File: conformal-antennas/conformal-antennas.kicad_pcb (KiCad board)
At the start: 2 copper layers, 1 part, among them J1 Conn_Coaxial

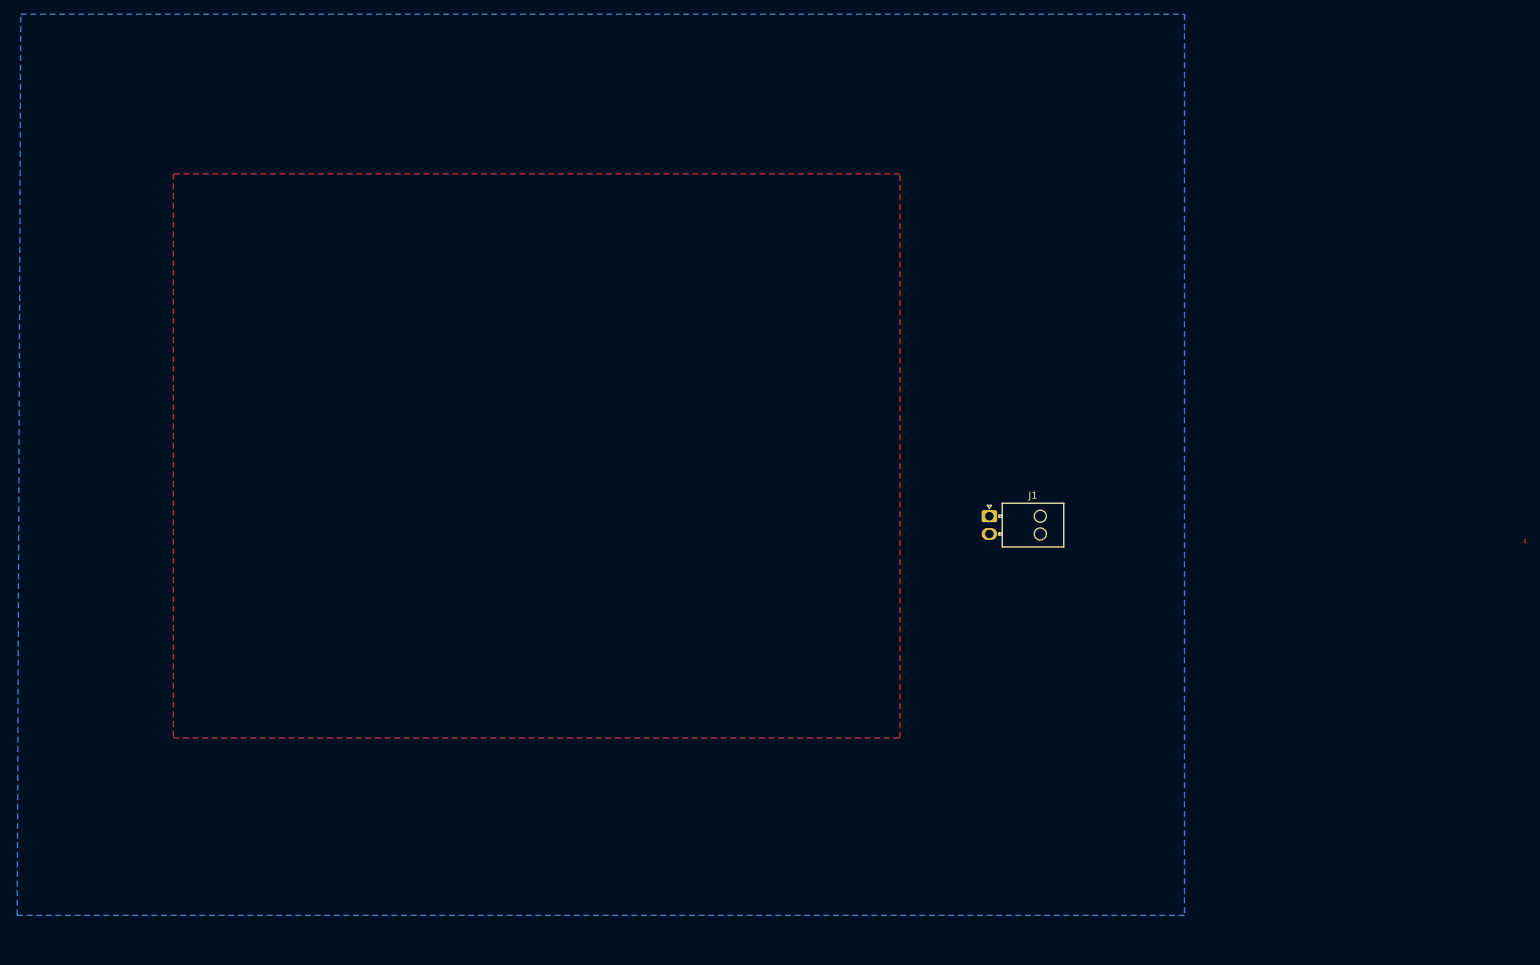
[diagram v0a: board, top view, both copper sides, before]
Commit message: changed coaxial connector to edge mount
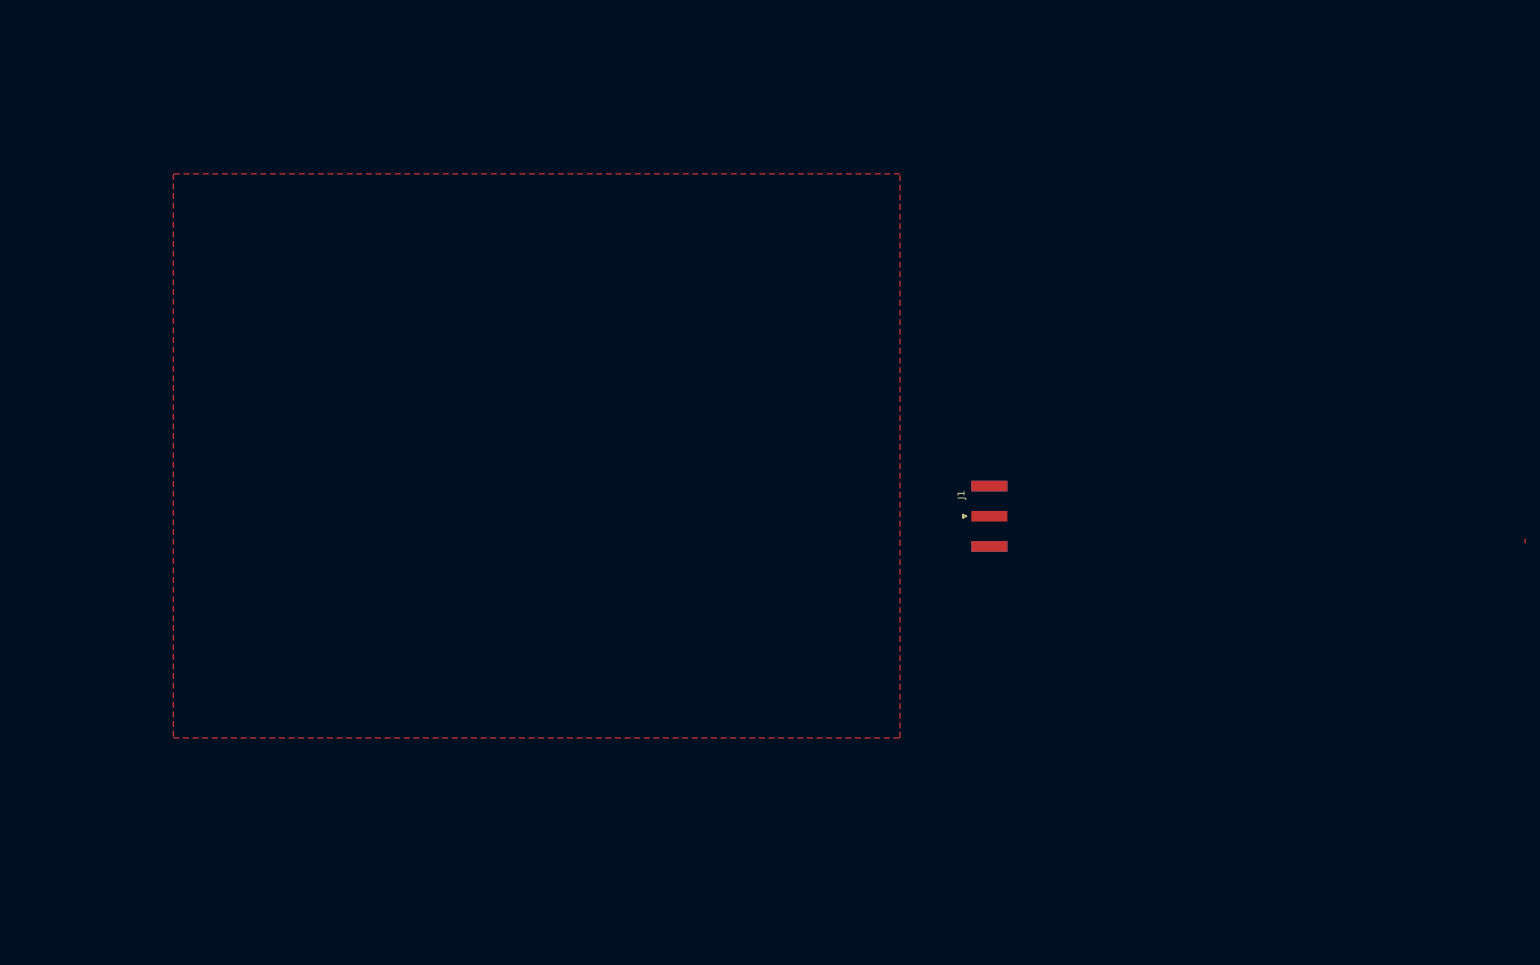
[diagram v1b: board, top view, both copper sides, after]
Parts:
- J1: footprint iclr:Molex_Nano-Fit_105313-xx02_1x02_P2.50mm_Horizontal -> Connector_Coaxial:SMA_Amphenol_132289_EdgeMount
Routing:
- removed copper zone on B.Cu, net GND

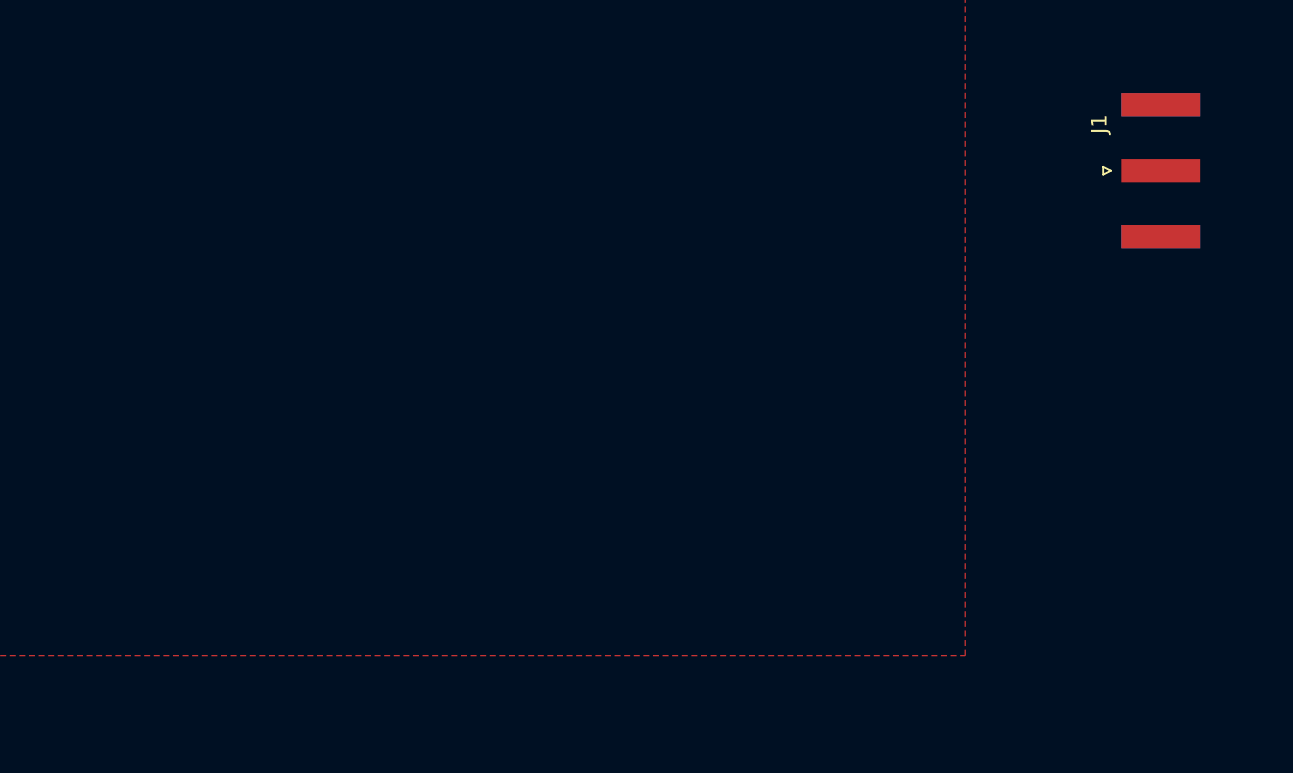
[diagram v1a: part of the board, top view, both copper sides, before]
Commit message: Simple path and tracks and SMA connector
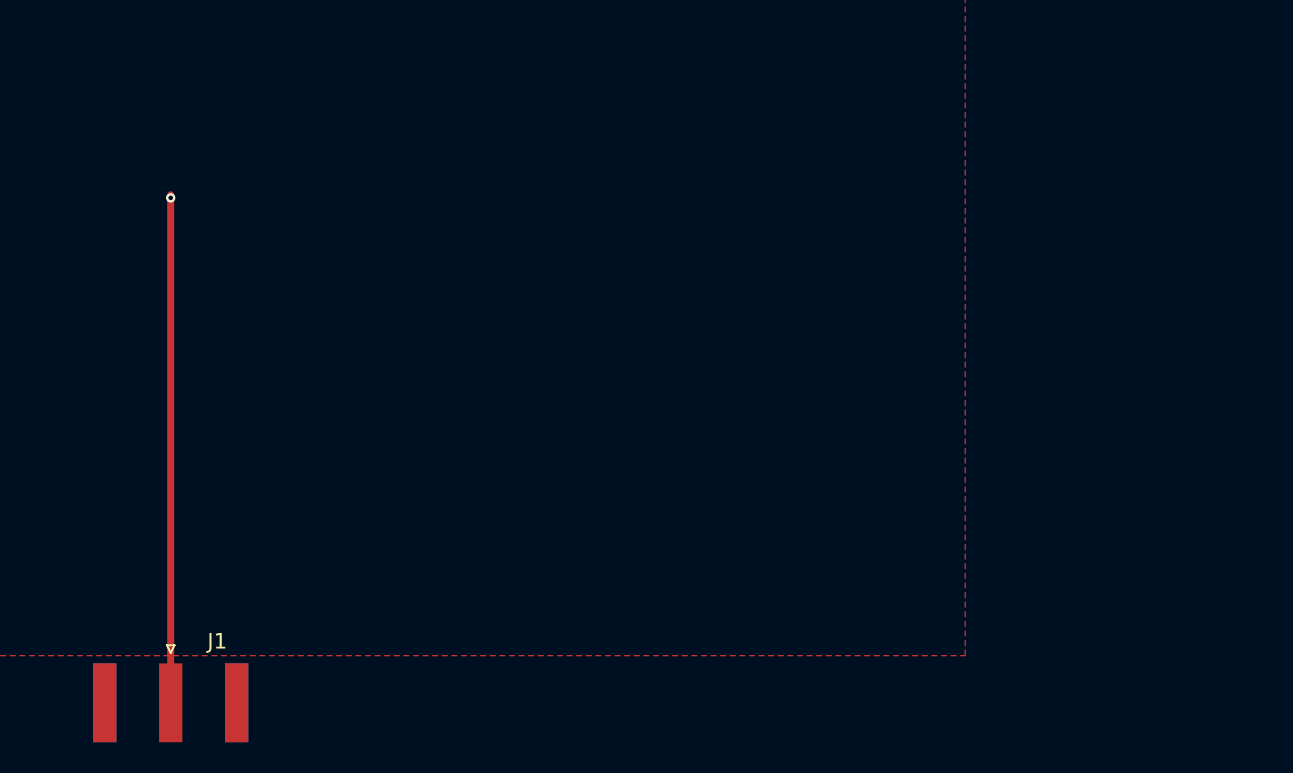
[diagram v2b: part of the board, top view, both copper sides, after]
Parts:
- moved J1 72.4 mm to (108.2, 149.5), turned to -90 degrees
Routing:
- net /Signal: track 0.00 -> 32.7 mm, vias 0 -> 1

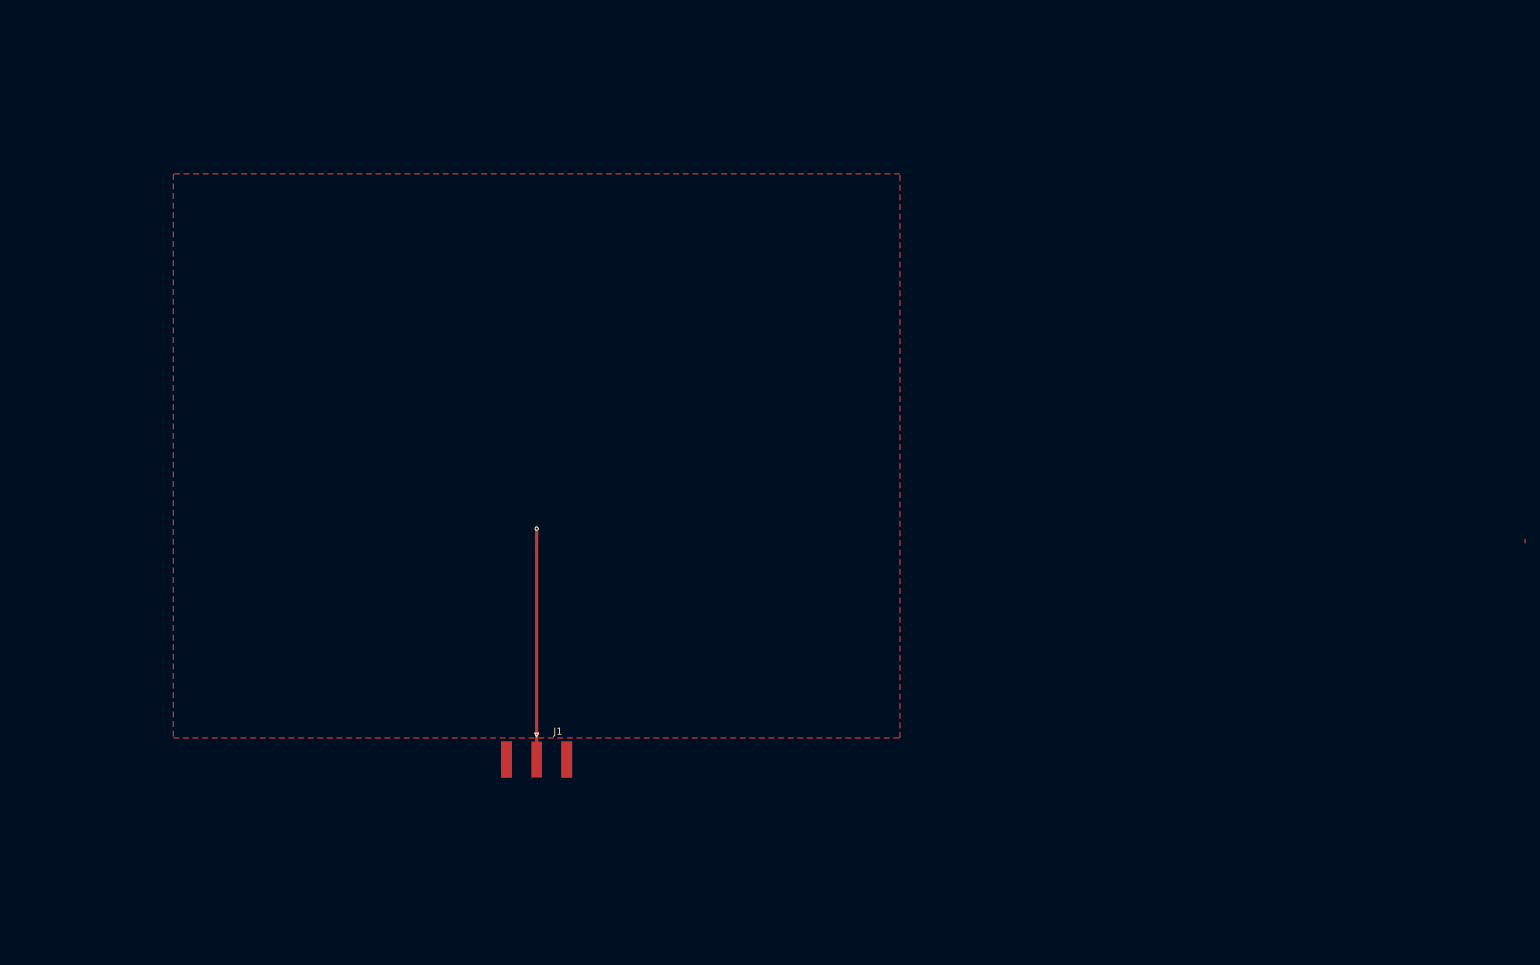
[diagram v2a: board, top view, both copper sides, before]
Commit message: Corrected simple path
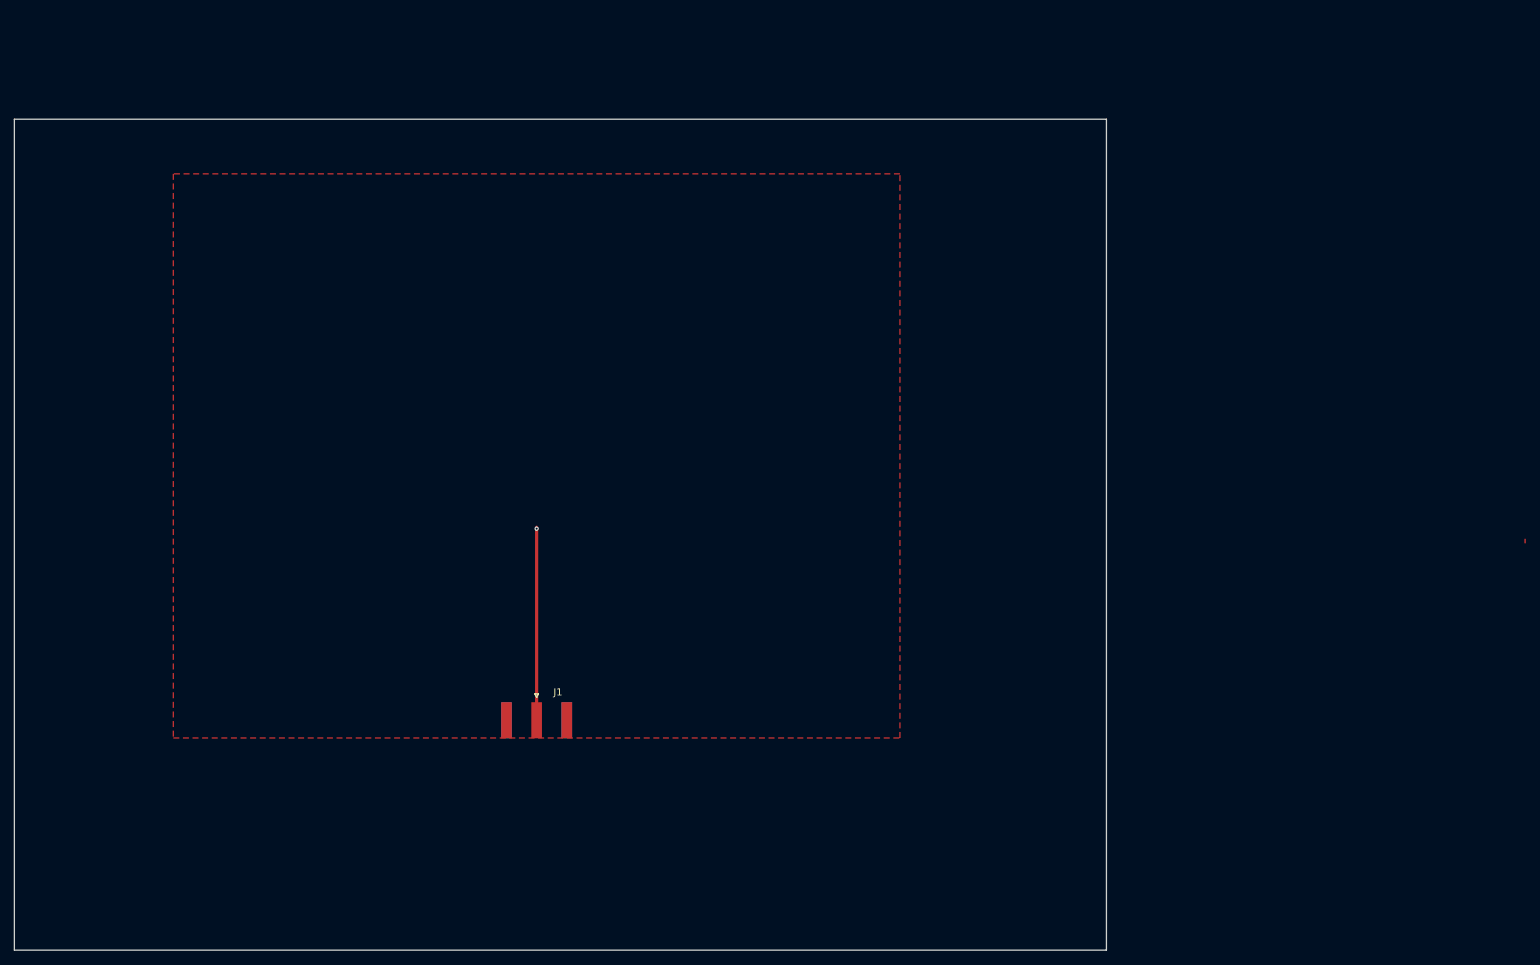
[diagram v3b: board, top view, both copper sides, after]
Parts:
- moved J1 5.54 mm to (108.2, 144.0)
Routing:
- net /Signal: track 32.7 -> 27.2 mm
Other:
- board outline added: 153.9 x 117.1 mm
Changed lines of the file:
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@@
 	(footprint "Connector_Coaxial:SMA_Amphenol_132289_EdgeMount"
 		(layer "F.Cu")
-		(at 108.2 149.5375 -90)
+		(at 108.2 144 -90)
 		(descr "https://www.amphenolrf.com/library/download/link/link_id/595984/parent/132289/")
 		(tags "SMA")
@@
 			)
 		)
+	)
+	(gr_rect
+		(start 34.6 59.3)
+		(end 188.5 176.4)
+		(stroke
+			(width 0.05)
+			(type default)
+		)
+		(fill no)
+		(layer "Edge.Cuts")
 	)
 	(segment
@@
 	)
 	(segment
-		(start 108.2 149.5375)
+		(start 108.2 144)
 		(end 108.2 117)
 		(width 0.45)
